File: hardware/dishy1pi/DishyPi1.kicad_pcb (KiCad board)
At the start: 4 copper layers, 93.4 x 69.3 mm, 99 parts, among them CN1 KF2EDGR-2.54-2P, CN2 KF2EDGR-2.54-9P, CN3 KF2EDGR-2.54-6P, CN4 KF2EDGR-2.54-4P, CN5 KF2EDGR-2.54-4P, CN6 KF2EDGR-2.54-9P, CN7 KF2EDGR-2.54-6P, J1 Conn_02x20_Odd_Even, SW1 SS-12F49-G050, U1 CAT24C256WI-GT3, U10 LTV-827S-TA1, U11 LTV-817S-TA1, U12 LTV-817S-TA1, U2 LTV-847S, U3 LTV-827S-TA1, U4 LTV-817S-TA1, U5 LTV-817S-TA1, U6 LTC4311ISC6#TRPBF, U7 ISO1540DR, U8 LM75BIMX-5/NOPB, U9 LTV-847S

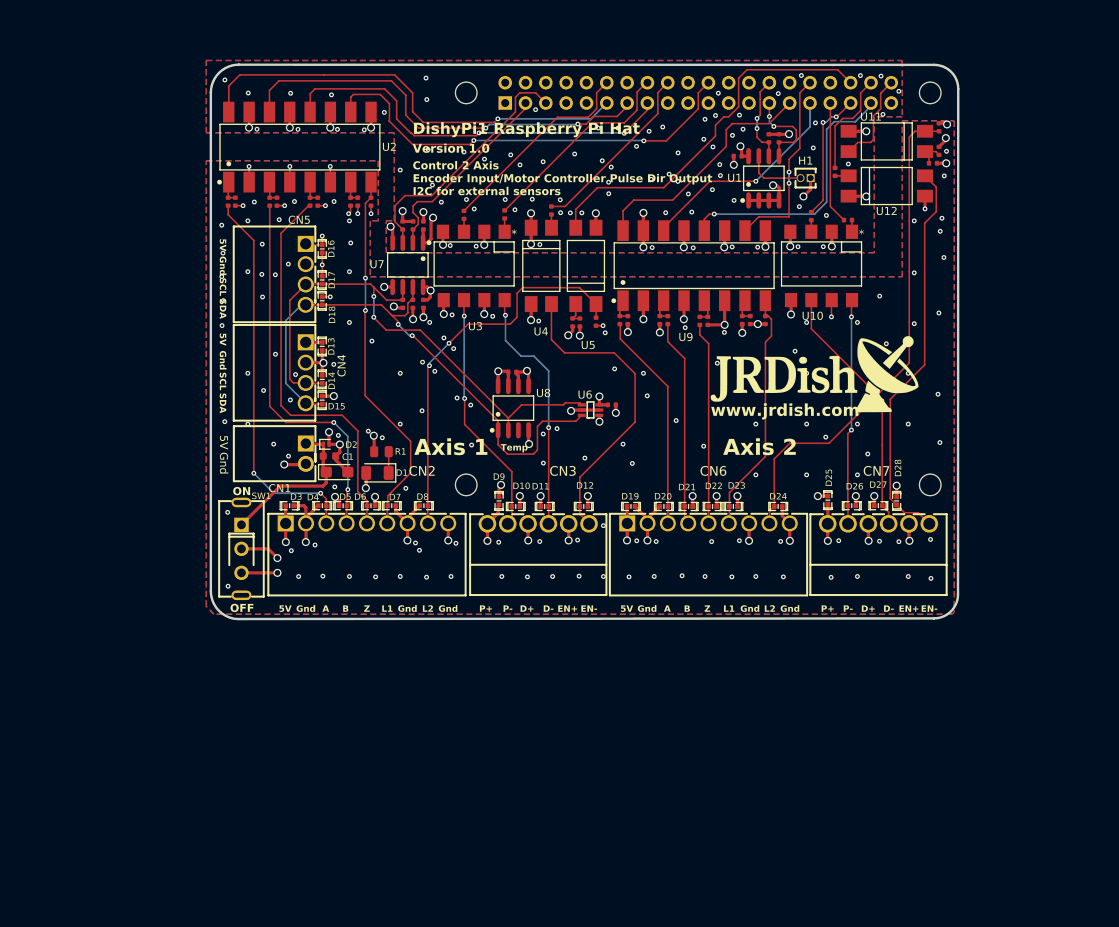
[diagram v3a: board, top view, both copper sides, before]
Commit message: Added power circuit to dishy schematic
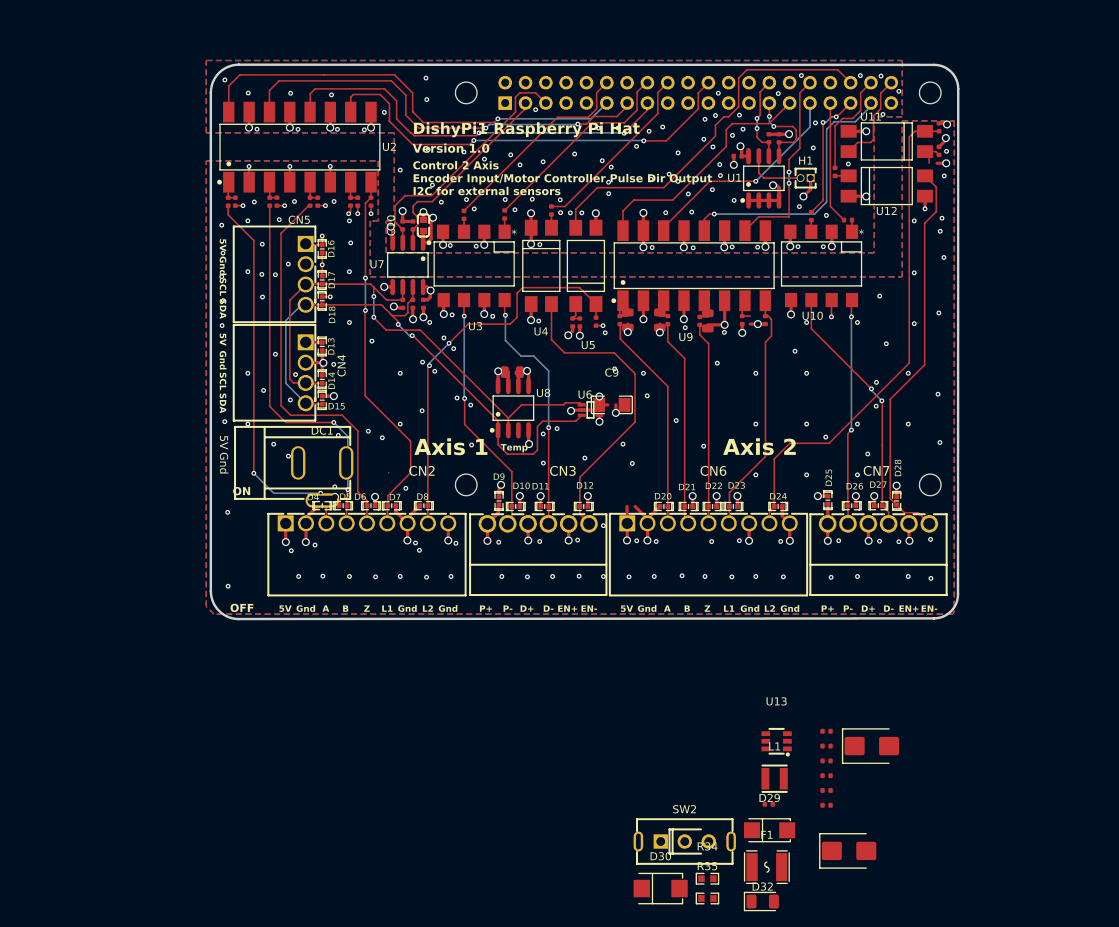
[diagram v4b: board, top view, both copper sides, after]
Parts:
- removed C1: 100nF, PCM_JLCPCB:C_0603
- removed C16, C17: 100pF, PCM_JLCPCB:C_0402
- removed C2: 10uF, PCM_JLCPCB:C_CASE-A-3216-18(mm)
- removed CN1: KF2EDGR-2.54-2P, MyParts:CONN-TH_P2.54_KF2EDGR-2.54-2P
- removed D1: LED, LED_SMD:LED_1206_3216Metric
- removed D19, D3: TPESD0402G05V, MyParts:D0402-BI
- removed D2: PESD5V0L1UL, Diode_SMD:D_SOD-882
- removed G***: LOGO, LOGO
- removed R1: 1kΩ, PCM_JLCPCB:R_0805
- removed SW1: SS-12F49-G050, MyParts:SW-TH_SS-12F45-GXXX
- added D29: SS34, PowerSupply:SMA_L4.3-W2.6-LS5.2-RD, F.Cu at (141.4, 139.7)
- added D30: SMBJ18A_C78412, MyParts:SMB_L4.6-W3.6-LS5.3-RD, F.Cu at (127.8, 147.0)
- added D32: LED, LED_SMD:LED_1206_3216Metric, F.Cu at (140.6, 148.6)
- added D33: SMBJ16A, PCM_JLCPCB:D_SMB, F.Cu at (154.2, 129.2)
- added D34: SMBJ16A, PCM_JLCPCB:D_SMB, F.Cu at (151.3, 142.2)
- added DC1: DC-005-2.5A-2.0, PowerSupply:CONN-TH_DC-005-2.5A-2.0, F.Cu at (85.5, 96.1)
- added F1: 1812L110/33MR, PowerSupply:F1812, F.Cu at (141.1, 144.3)
- added L1: 4.7uH, PowerSupply:IND-SMD_L3.0-W3.0-1, F.Cu at (142.0, 133.2)
- added R28: 22kΩ, PCM_JLCPCB:R_0402, F.Cu at (148.5, 127.3)
- added R29: 1kΩ, PCM_JLCPCB:R_0402, F.Cu at (148.5, 129.2)
- added R30: 1kΩ, PCM_JLCPCB:R_0402, F.Cu at (148.5, 131.0)
- added R31: 1kΩ, PCM_JLCPCB:R_0402, F.Cu at (148.5, 132.8)
- added R32: 470Ω, PCM_JLCPCB:R_0402, F.Cu at (148.5, 134.7)
- added R33: 22kΩ, PCM_JLCPCB:R_0402, F.Cu at (148.5, 136.6)
- added R34: 54.9k, PowerSupply:R0603, F.Cu at (133.7, 145.7)
- added R35: 10k, PowerSupply:R0603, F.Cu at (133.7, 148.2)
- added R36: 2.2kΩ, PCM_JLCPCB:R_0402, F.Cu at (141.3, 136.4)
- added SW2: SS-12F49-G050, PowerSupply:SW-TH_SS-12F45-GXXX, F.Cu at (130.8, 141.1)
- added U13: TPS561201DDCR, PowerSupply:SOT-23-6_L2.9-W1.6-P0.95-LS2.8-BR, F.Cu at (142.3, 128.6)
- C10: footprint PCM_JLCPCB:C_0402 -> PowerSupply:C0603
- C12: value 100nF -> 10uF; footprint PCM_JLCPCB:C_0402 -> PCM_JLCPCB:C_0805
- C13, C14: value 100pF -> 10uF; footprint PCM_JLCPCB:C_0402 -> PCM_JLCPCB:C_0805
- C15: value 100pF -> 100nF; footprint PCM_JLCPCB:C_0402 -> PCM_JLCPCB:C_0805
- C5, C6, C7, C8: value 100pF -> 100nF
- C9: value 100nF -> 47uF; footprint PCM_JLCPCB:C_0402 -> PowerSupply:C1206
- R10: value 1kΩ -> 220Ω
- R11: value 1kΩ -> 22kΩ
- R12: value 470Ω -> 1kΩ
- R13, R8: value 22kΩ -> 1kΩ
- R14: value 4.7kΩ -> 1kΩ
- R15: value 4.7kΩ -> 470Ω
- R16: value 4.7kΩ -> 22kΩ
- R18, R19, R20: value 1kΩ -> 4.7kΩ
- R21: value 220Ω -> 1kΩ
- R22: value 22kΩ -> 10kΩ
- R24, R5, R9: value 1kΩ -> 10kΩ
- R26: value 470Ω -> 10kΩ
- R27: value 22kΩ -> 220Ω
- R7: value 220Ω -> 10kΩ
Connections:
- C10 pad 1: +3.3V -> 12V_PROT
- C10 pad 2: GNDPI -> GNDIO
- C11 pad 1: +5V -> Net-(U13-VBST)
- C11 pad 2: GNDIO -> /12v_in/VBST-SW-L1
- C13 pad 1: GNDIO -> +5V
- C13 pad 2: Net-(U9-AN1) -> GNDIO
- C14 pad 1: GNDIO -> 12V_PROT
- C14 pad 2: Net-(U9-AN2) -> GNDIO
- C15 pad 1: GNDIO -> 12V_PROT
- C15 pad 2: Net-(U9-AN3) -> GNDIO
- C4 pad 1: GNDIO -> Net-(U2-AN4)
- C4 pad 2: Net-(U2-AN1) -> GNDIO
- C5 pad 1: GNDIO -> +5V
- C5 pad 2: Net-(U2-AN2) -> GNDIO
- C6 pad 1: GNDIO -> +3.3V
- C6 pad 2: Net-(U2-AN3) -> GNDPI
- C7 pad 1: Net-(U2-AN4) -> +5V
- C8 pad 1: Net-(C8-Pad1) -> +5V
- C9 pad 1: +5V -> 12V_PROT
- CN2 pad 1: +5V -> 12V_PROT
- CN6 pad 1: +5V -> 12V_PROT
- R10 pad 1: E_DIR/23 -> +5V
- R10 pad 2: Net-(R10-Pad2) -> Net-(U2-AN4)
- R11 pad 1: E_MF/24 -> /IO/LIM_1
- R11 pad 2: Net-(R11-Pad2) -> GNDIO
- R12 pad 1: +5V -> E_DIR/23
- R12 pad 2: Net-(C8-Pad1) -> Net-(R12-Pad2)
- R13 pad 1: /IO/LIM_2 -> E_PUL/18
- R13 pad 2: GNDIO -> Net-(R13-Pad2)
- R14 pad 1: +3.3V -> E_MF/24
- R14 pad 2: PI_SCL -> Net-(R14-Pad2)
- R15 pad 1: +3.3V -> +5V
- R15 pad 2: PI_SDA -> Net-(R15-Pad2)
- R16 pad 1: +5V -> /IO/LIM_2
- R16 pad 2: /I2C/SDA -> +5V
- R17 pad 1: +5V -> +3.3V
- R17 pad 2: /I2C/SCL -> PI_SCL
- R18 pad 1: /io2/ENC_Z -> +3.3V
- R18 pad 2: Net-(U9-AN3) -> PI_SDA
- R19 pad 1: /io2/ENC_B -> +5V
- R19 pad 2: Net-(U9-AN2) -> /I2C/SDA
- R20 pad 1: /io2/ENC_A -> +5V
- R20 pad 2: Net-(U9-AN1) -> /I2C/SCL
- R21 pad 2: Net-(U9-AN4) -> Net-(U9-AN3)
- R22 pad 1: /io2/LIM_1 -> +5V
- R22 pad 2: GNDIO -> /io2/ENC_Z
- R23 pad 1: A_PUL/13 -> +5V
- R23 pad 2: Net-(R23-Pad2) -> Net-(U9-AN2)
- R24 pad 1: A_DIR/19 -> +5V
- R24 pad 2: Net-(R24-Pad2) -> /io2/ENC_B
- R25 pad 1: A_MF/20 -> +5V
- R25 pad 2: Net-(R25-Pad2) -> Net-(U9-AN1)
- R26 pad 2: Net-(C17-Pad1) -> /io2/ENC_A
- R27 pad 1: /io2/LIM_2 -> +5V
- R27 pad 2: GNDIO -> Net-(U9-AN4)
- R4 pad 1: /IO/ENC_Z -> +5V
- R5 pad 1: /IO/ENC_B -> +5V
- R5 pad 2: Net-(U2-AN2) -> /IO/ENC_Z
- R6 pad 1: /IO/ENC_A -> +5V
- R6 pad 2: Net-(U2-AN1) -> Net-(U2-AN2)
- R7 pad 2: Net-(U2-AN4) -> /IO/ENC_B
- R8 pad 1: /IO/LIM_1 -> +5V
- R8 pad 2: GNDIO -> Net-(U2-AN1)
- R9 pad 1: E_PUL/18 -> +5V
- R9 pad 2: Net-(R9-Pad2) -> /IO/ENC_A
- U10 pad 1: Net-(R23-Pad2) -> Net-(R29-Pad2)
- U10 pad 3: Net-(R24-Pad2) -> Net-(R30-Pad2)
- U11 pad 1: Net-(R25-Pad2) -> Net-(R31-Pad2)
- U12 pad 1: Net-(C17-Pad1) -> Net-(R32-Pad2)
- U2 pad 2: GNDIO -> /IO/ENC_A
- U2 pad 4: GNDIO -> /IO/ENC_B
- U2 pad 6: GNDIO -> /IO/ENC_Z
- U3 pad 1: Net-(R10-Pad2) -> Net-(R12-Pad2)
- U3 pad 3: Net-(R9-Pad2) -> Net-(R13-Pad2)
- U4 pad 1: Net-(R11-Pad2) -> Net-(R14-Pad2)
- U5 pad 1: Net-(C8-Pad1) -> Net-(R15-Pad2)
- U9 pad 2: GNDIO -> /io2/ENC_A
- U9 pad 4: GNDIO -> /io2/ENC_B
- U9 pad 6: GNDIO -> /io2/ENC_Z
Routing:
- net GNDIO: track 131.2 -> 93.5 mm, vias 196 -> 178
- net Net-(D2-K): track 20.0 -> 0.00 mm
- net +5V: track 57.5 -> 41.7 mm, vias 21 -> 15
- net 12V_PROT: track 0.00 -> 7.66 mm, vias 0 -> 3
- net /io2/ENC_B: track 26.0 -> 29.8 mm, vias 0 -> 1
- net (no net): track 0.00 -> 3.62 mm
- net Net-(C17-Pad1): track 3.60 -> 0.00 mm
- net /IO/ENC_A: track 48.2 -> 51.8 mm, vias 2 -> 3
- net Net-(C8-Pad1): track 2.86 -> 0.00 mm
- net Net-(D1-K): track 2.65 -> 0.00 mm
- net Net-(U2-AN4): track 2.85 -> 5.47 mm, vias 0 -> 1
- net /io2/ENC_A: track 27.4 -> 29.7 mm, vias 0 -> 1
- net +3.3V: track 15.6 -> 17.8 mm, vias 5 -> 7
- net /IO/ENC_Z: track 49.7 -> 51.7 mm, vias 0 -> 1
- net /IO/ENC_B: track 47.4 -> 49.3 mm, vias 2 -> 3
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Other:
- board text removed: "www.jrdish.com"

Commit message: New PCB layout started
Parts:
- moved D34 83.3 mm to (76.2, 106.3), turned to -90 degrees
- moved F1 74.2 mm to (95.5, 85.8), turned to -90 degrees
- moved SW2 70.2 mm to (90.0, 84.0), turned to 90 degrees
- moved U13 62.5 mm to (89.7, 94.7)
- moved L1 60.4 mm to (95.5, 94.8)
- moved C9 47.5 mm to (115.0, 133.5)
- moved D33 43.2 mm to (123.5, 98.7), turned to 90 degrees
- moved C12 21.0 mm to (90.0, 74.0)
- moved U6 9.54 mm to (110.8, 82.2)
- moved U8 6.80 mm to (106.1, 81.0)
- moved DC1 4.31 mm to (81.3, 97.0)
- moved CN4 4.05 mm to (79.4, 82.5)
- moved CN5 4.05 mm to (79.4, 70.2)
- moved D13 4.05 mm to (81.5, 79.2)
- moved D14 4.05 mm to (81.5, 83.3)
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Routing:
- net GNDIO: track 93.5 -> 0.00 mm, vias 178 -> 0
- net /I2C/SDA: track 70.6 -> 0.00 mm, vias 2 -> 0
- net /I2C/SCL: track 69.0 -> 0.00 mm, vias 2 -> 0
- net /io2/LIM_2: track 62.4 -> 0.00 mm
- net E_ENC_A/17: track 56.0 -> 0.00 mm, vias 1 -> 0
- net E_LIM_1/25: track 55.0 -> 0.00 mm, vias 2 -> 0
- net E_ENC_B/22: track 53.4 -> 0.00 mm, vias 2 -> 0
- net /IO/ENC_A: track 51.8 -> 0.00 mm, vias 3 -> 0
- net /IO/ENC_Z: track 51.7 -> 0.00 mm, vias 1 -> 0
- net E_ENC_Z/27: track 51.1 -> 0.00 mm, vias 2 -> 0
- net /IO/LIM_2: track 50.7 -> 0.00 mm, vias 3 -> 0
- net /io2/MF-: track 49.5 -> 0.00 mm
- net /IO/ENC_B: track 49.3 -> 0.00 mm, vias 3 -> 0
- net E_LIM_2/16: track 47.5 -> 0.00 mm
- net /IO/LIM_1: track 46.5 -> 0.00 mm, vias 2 -> 0
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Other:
- board size 93.4 x 69.3 mm -> 94.6 x 69.3 mm
- board text removed: "Axis 1"
- board text removed: "Axis 2"
- board text removed: "OFF"
- board text removed: "ON"

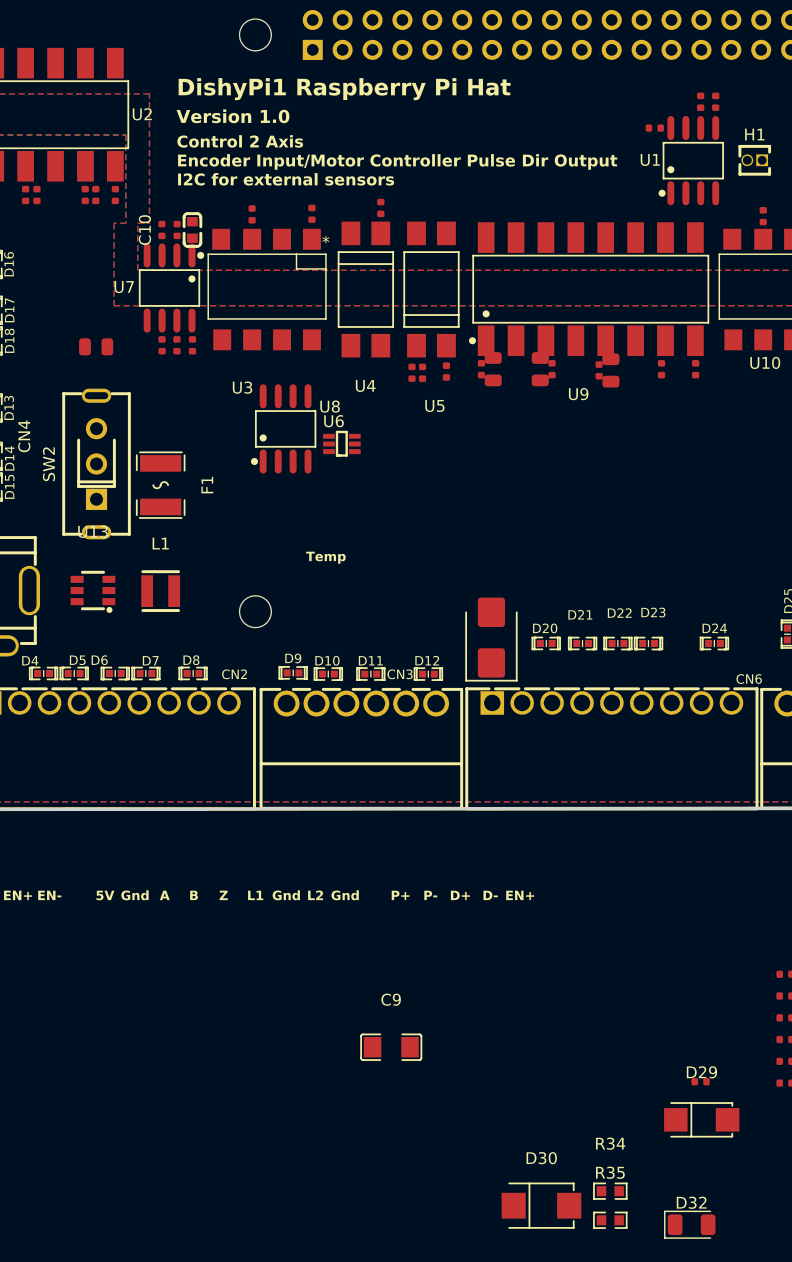
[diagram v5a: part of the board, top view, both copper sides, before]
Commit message: Added 12V power input
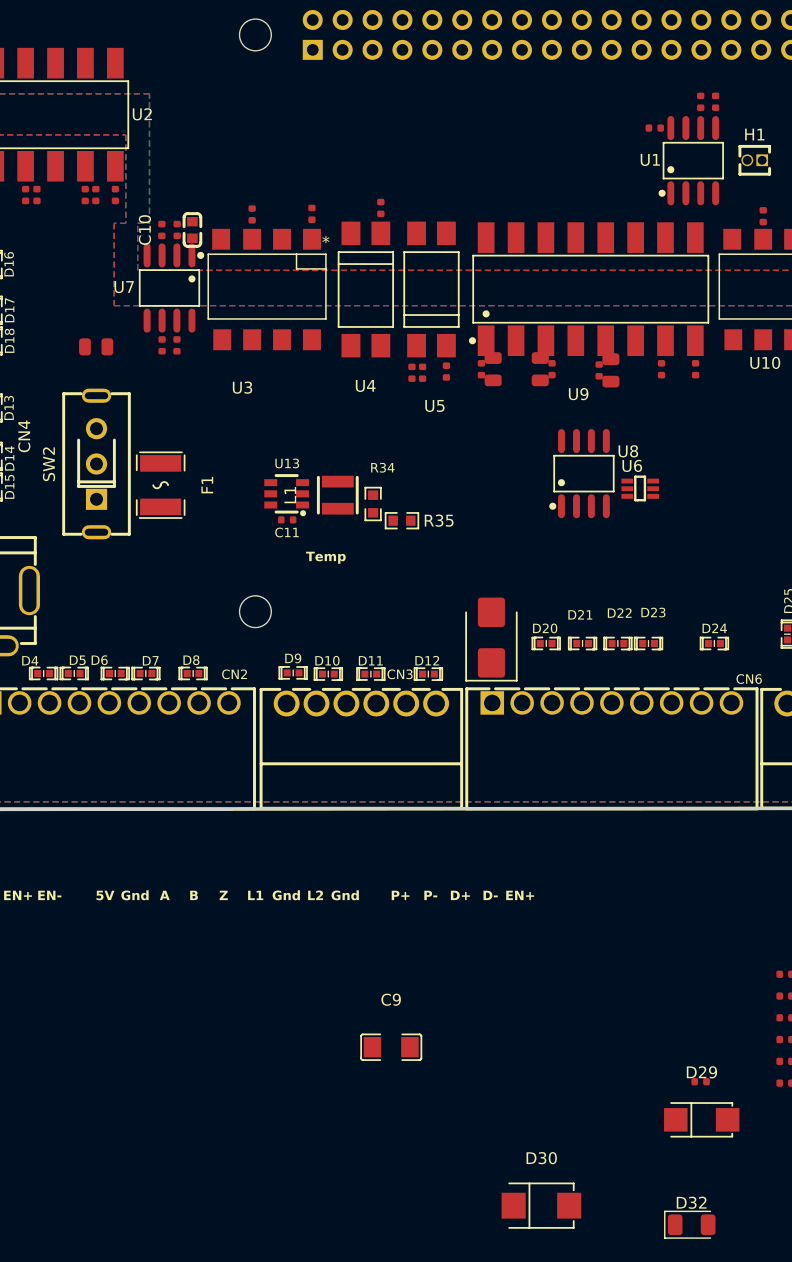
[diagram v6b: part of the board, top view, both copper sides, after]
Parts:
- moved R35 62.0 mm to (116.0, 88.8)
- moved R34 61.8 mm to (113.5, 87.3), turned to 90 degrees
- moved U6 25.6 mm to (136.2, 86.0)
- moved U8 25.6 mm to (131.4, 84.8)
- moved U13 18.4 mm to (106.2, 86.5)
- moved L1 17.1 mm to (110.5, 86.6), turned to 90 degrees
- moved C11 16.9 mm to (106.2, 88.7), turned to 0 degrees
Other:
- board text removed: "Control 2 Axis Encoder Input/Motor Controller Pulse Dir Output I2C for external sensors"
- board text removed: "DishyPi1 Raspberry Pi Hat"
- board text removed: "Version 1.0"
